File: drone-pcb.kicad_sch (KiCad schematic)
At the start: 42 parts, among them J1 Conn_01x02_Pin, J10 Conn_01x03_Pin, J2 Conn_01x02_Pin, J3 Conn_01x02_Pin, J4 Conn_01x02_Pin, J5 USB_C_Receptacle_USB2.0_16P, J6 Conn_01x02_Pin, J7 Conn_01x03_Pin, J8 Conn_01x03_Pin, J9 Conn_01x03_Pin, Q1 AO3400A, Q2 AO3400A, Q3 AO3400A, Q4 AO3400A, Q5 AO3400A, Q6 AO3400A, SW2 SW_Push_Dual_x2, U1 STM32F103C8Tx, U2 TLV75533PDBV, U3 MPU-9250, U4 MCP73831-2-OT, U5 nRF24L01P, U6 DW01A, Y1 Crystal

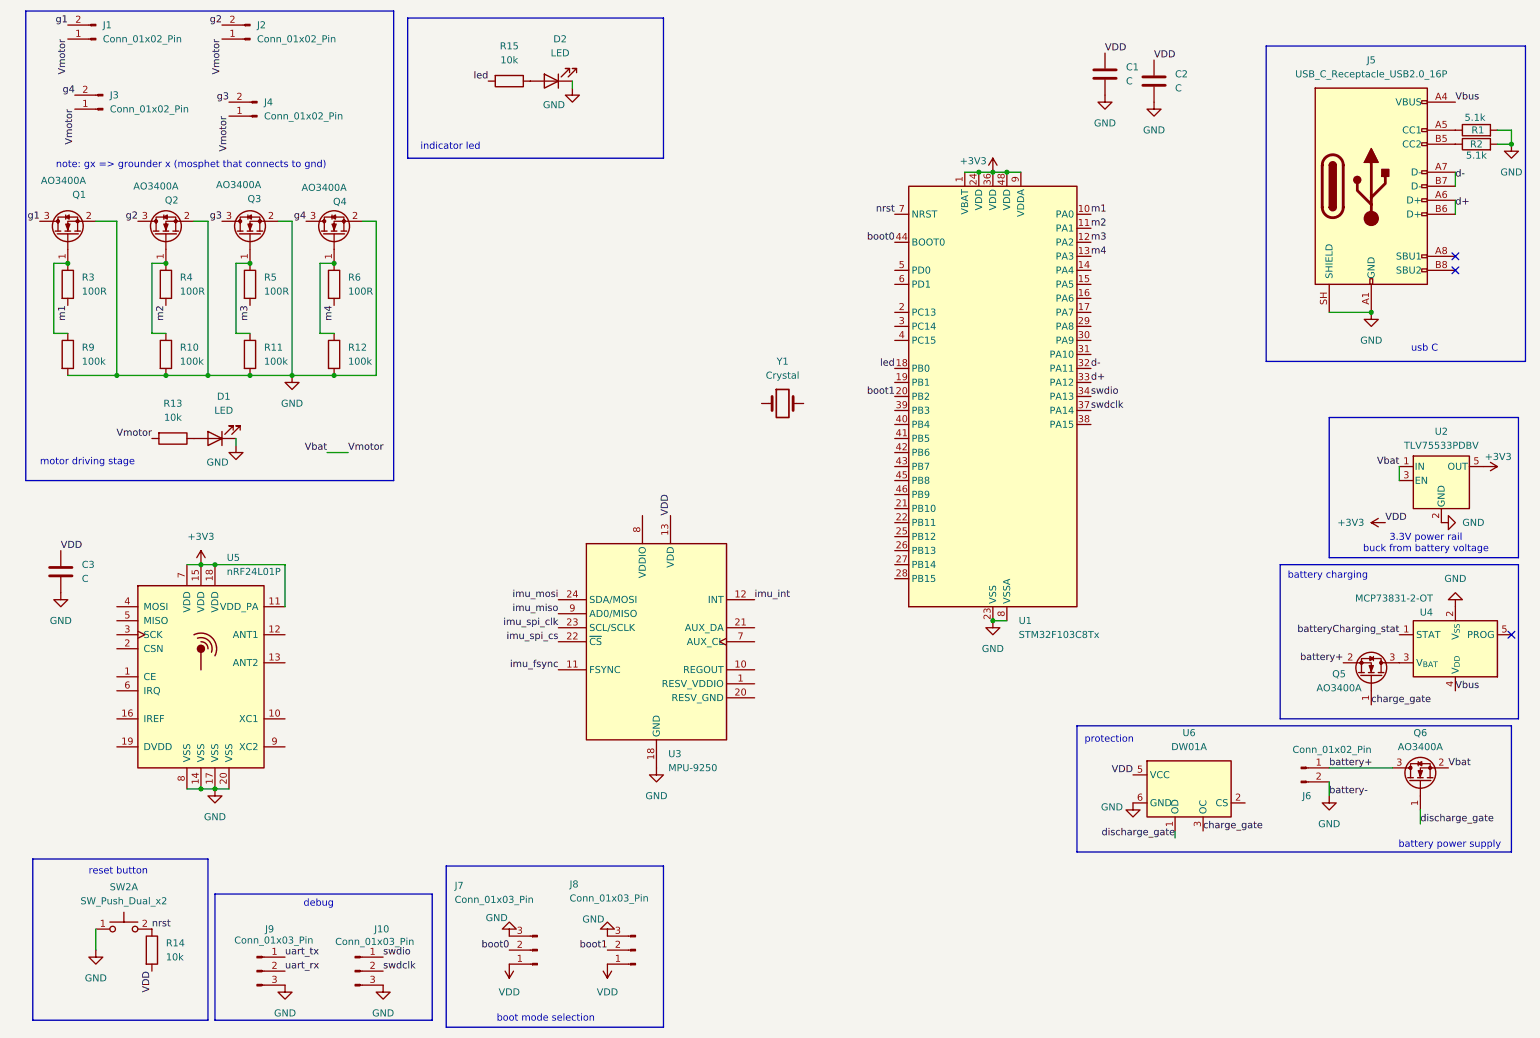
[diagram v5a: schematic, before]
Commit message: connect nrf24l01+ and mpu6050
add resistor to prog pin in lipo charger, add d+ pullup to the stm32, add input and output voltage capacitors to lipo charger
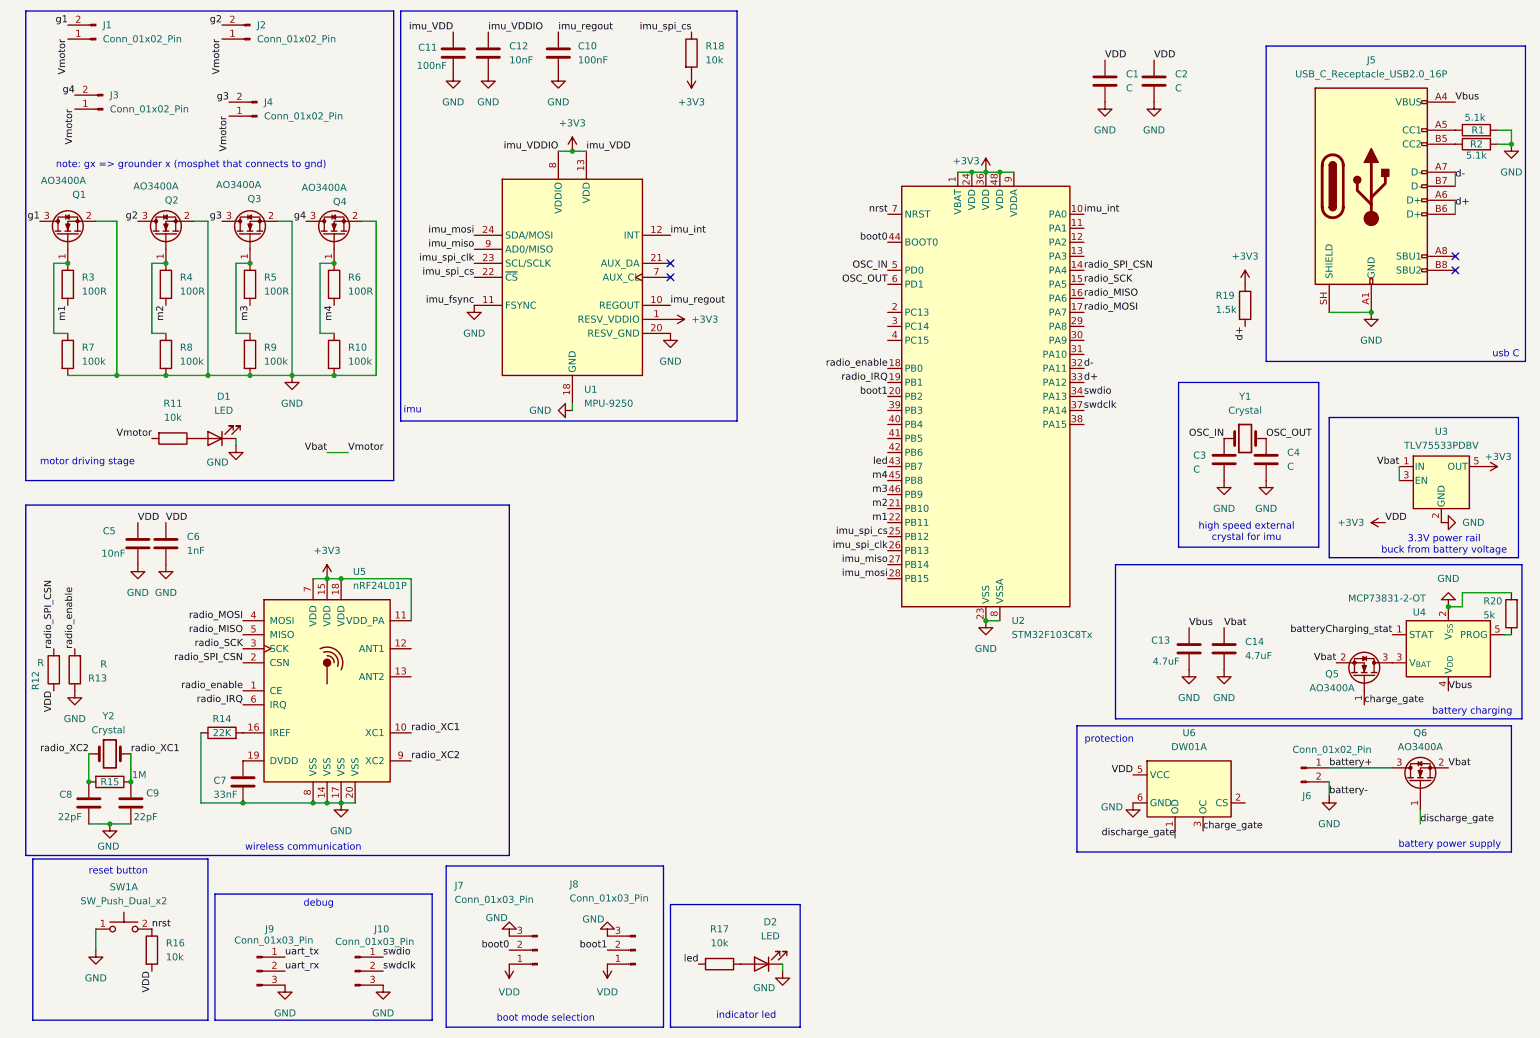
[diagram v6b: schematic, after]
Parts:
- added C10, C11: 100nF, Capacitor_SMD:C_0805_2012Metric_Pad1.18x1.45mm_HandSolder, symbol Device:C
- added C12: 10nF, Capacitor_SMD:C_0805_2012Metric_Pad1.18x1.45mm_HandSolder, symbol Device:C
- added C13, C14: 4.7uF, Capacitor_SMD:C_0805_2012Metric_Pad1.18x1.45mm_HandSolder, symbol Device:C
- added C3, C4: C, Capacitor_SMD:C_0805_2012Metric_Pad1.18x1.45mm_HandSolder, symbol Device:C
- added C6: 1nF, Capacitor_SMD:C_0805_2012Metric_Pad1.18x1.45mm_HandSolder, symbol Device:C
- added C7: 33nF, Capacitor_SMD:C_0805_2012Metric_Pad1.18x1.45mm_HandSolder, symbol Device:C
- added C8, C9: 22pF, Capacitor_SMD:C_0805_2012Metric_Pad1.18x1.45mm_HandSolder, symbol Device:C
- added R12, R13: R, Resistor_SMD:R_0603_1608Metric_Pad0.98x0.95mm_HandSolder, symbol Device:R
- added R14: 22K, Resistor_SMD:R_0603_1608Metric_Pad0.98x0.95mm_HandSolder, symbol Device:R
- added R15: 1M, Resistor_SMD:R_0603_1608Metric_Pad0.98x0.95mm_HandSolder, symbol Device:R
- added R18: 10k, symbol Device:R
- added R19: 1.5k, symbol Device:R
- added R20: 5k, symbol Device:R
- added Y2: Crystal, symbol Device:Crystal
- C5: renamed from C3; value C -> 10nF
- R1, R2, R3, R4, R5, R6: footprint Resistor_SMD:R_0805_2012Metric_Pad1.20x1.40mm_HandSolder -> Resistor_SMD:R_0603_1608Metric_Pad0.98x0.95mm_HandSolder
- R10: renamed from R12; footprint Resistor_SMD:R_0805_2012Metric_Pad1.20x1.40mm_HandSolder -> Resistor_SMD:R_0603_1608Metric_Pad0.98x0.95mm_HandSolder
- R11: renamed from R13; footprint Resistor_SMD:R_0805_2012Metric_Pad1.20x1.40mm_HandSolder -> Resistor_SMD:R_0603_1608Metric_Pad0.98x0.95mm_HandSolder
- R16: renamed from R14; footprint Resistor_SMD:R_0805_2012Metric_Pad1.20x1.40mm_HandSolder -> Resistor_SMD:R_0603_1608Metric_Pad0.98x0.95mm_HandSolder
- R17: renamed from R15; footprint Resistor_SMD:R_0805_2012Metric_Pad1.20x1.40mm_HandSolder -> Resistor_SMD:R_0603_1608Metric_Pad0.98x0.95mm_HandSolder
- R7: renamed from R9; footprint Resistor_SMD:R_0805_2012Metric_Pad1.20x1.40mm_HandSolder -> Resistor_SMD:R_0603_1608Metric_Pad0.98x0.95mm_HandSolder
- R8: renamed from R10; footprint Resistor_SMD:R_0805_2012Metric_Pad1.20x1.40mm_HandSolder -> Resistor_SMD:R_0603_1608Metric_Pad0.98x0.95mm_HandSolder
- R9: renamed from R11; footprint Resistor_SMD:R_0805_2012Metric_Pad1.20x1.40mm_HandSolder -> Resistor_SMD:R_0603_1608Metric_Pad0.98x0.95mm_HandSolder
- renumbered SW2 to SW1, U3 to U1, U1 to U2, U2 to U3
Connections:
- net imu_fsync is gone; now on net GND: U1.11 (FSYNC)
- net +3V3: now also U1.1 (RESV_VDDIO), U1.8 (VDDIO), C11.1, C12.1, C6.1, R12.1, R18.2, R19.1
- net GND: now also U1.20 (RESV_GND), C10.2, C11.2, C12.2, C13.2, C14.2, C3.2, C4.2, C6.2, C7.2, C8.2, C9.2, R13.1, R14.1, R20.2
- net Vbat: now also Q5.2 (S), C14.1
- net Vbus: now also C13.1
- net battery+: no longer Q5.2 (S)
- net d+: now also R19.2
- net imu_int: now also U2.10 (PA0)
- net imu_miso: now also U2.27 (PB14)
- net imu_mosi: now also U2.28 (PB15)
- net imu_spi_clk: now also U2.26 (PB13)
- net imu_spi_cs: now also U2.25 (PB12), R18.1
- net led: now also U2.43 (PB7); no longer U2.18 (PB0)
- net m1: now also U2.22 (PB11); no longer U2.10 (PA0)
- net m2: now also U2.21 (PB10); no longer U2.11 (PA1)
- net m3: now also U2.46 (PB9); no longer U2.12 (PA2)
- net m4: now also U2.45 (PB8); no longer U2.13 (PA3)
- net imu_regout: now reaches U1.10 (REGOUT)
- net imu_regout: now also C10.1
- net radio_SPI_CSN: now reaches U2.14 (PA4)
- net radio_SPI_CSN: now also U5.2 (CSN), R12.2
- net radio_SCK: now reaches U2.15 (PA5)
- net radio_SCK: now also U5.3 (SCK)
- net radio_MISO: now reaches U2.16 (PA6)
- net radio_MISO: now also U5.5 (MISO)
- net radio_MOSI: now reaches U2.17 (PA7)
- net radio_MOSI: now also U5.4 (MOSI)
- net radio_IRQ: now reaches U2.19 (PB1)
- net radio_IRQ: now also U5.6 (IRQ)
- net OSC_IN: now reaches U2.5 (PD0)
- net OSC_IN: now also Y1.1, C3.1
- net OSC_OUT: now reaches U2.6 (PD1)
- net OSC_OUT: now also Y1.2, C4.1
- net radio_enable: now reaches U5.1 (CE)
- net radio_enable: now also U2.18 (PB0), R13.2
- net radio_XC1: now reaches U5.10 (XC1)
- net radio_XC1: now also C9.1, R15.1, Y2.2
- net at U5.16 (IREF): now also R14.2
- net at U5.19 (DVDD): now also C7.1
- net radio_XC2: now reaches U5.9 (XC2)
- net radio_XC2: now also C8.1, R15.2, Y2.1
- net at U4.5 (PROG): now also R20.1
- no-connect marks 3 -> 4
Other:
- note added: "high speed external crystal for imu"
- note added: "imu"
- note added: "wireless communication"
- moved on the sheet: C1, C5, D2, Q5, R17, U1, U2, U4, U5, Y1
